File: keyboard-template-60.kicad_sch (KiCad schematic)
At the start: 168 parts, among them J1 USB_C_Receptacle_USB2.0, J2 Conn_01x04_MountingPin, SW1 SW_Reset, U1 ATmega32U4-M, U2 SRV05-4, Y1 16MHz

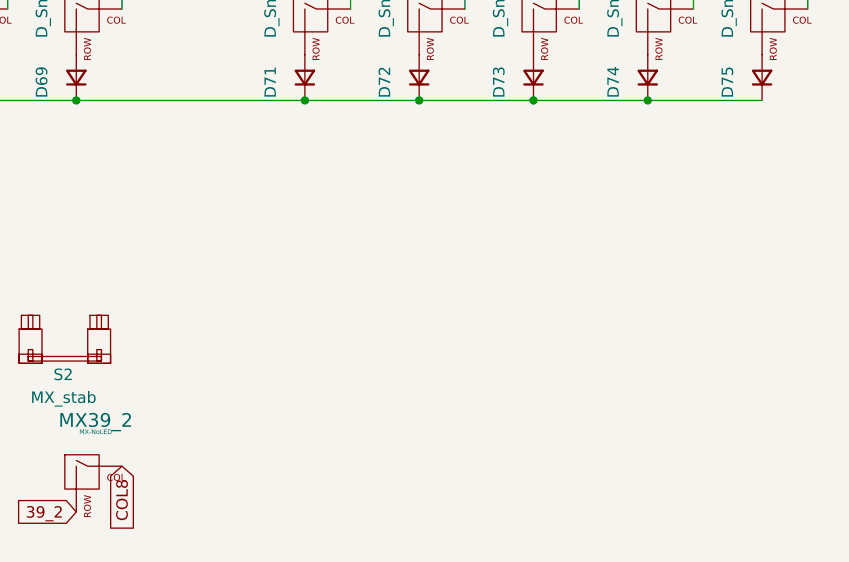
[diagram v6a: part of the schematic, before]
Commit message: Add mounting holes and re-export productions files
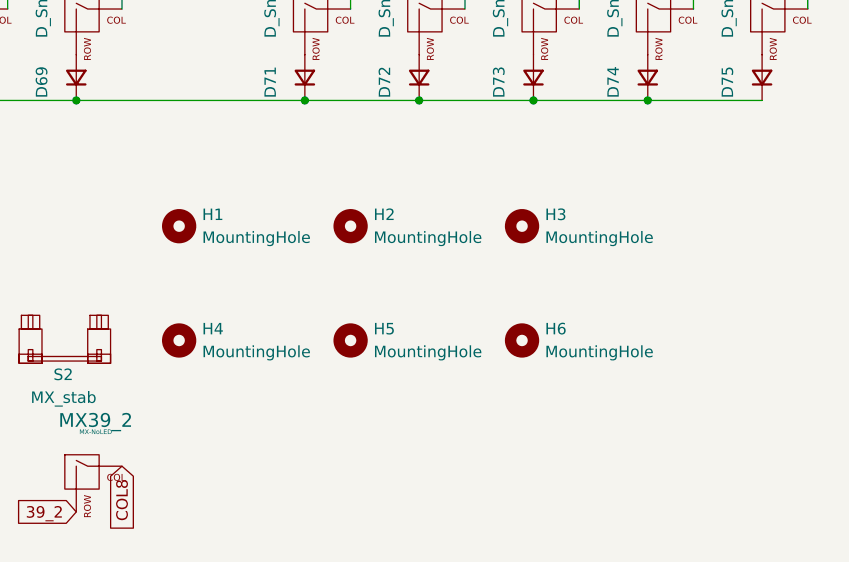
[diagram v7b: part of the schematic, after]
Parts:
- added H1, H2, H3, H4, H5, H6: MountingHole, MountingHole:MountingHole_2.2mm_M2_Pad_TopOnly, symbol Mechanical:MountingHole
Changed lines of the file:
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@@
     (pin "2")
+  )
+  (symbol (lib_id "Mechanical:MountingHole") (at 203.2 241.3 0) (unit 1)
+    (in_bom yes) (on_board yes) (fields_autoplaced)
+    (property "Reference" "H6" (id 0) (at 205.74 240.0299 0)
+      (effects (font (size 1.27 1.27)) (justify left))
+    )
+    (property "Value" "MountingHole" (id 1) (at 205.74 242.5699 0)
+      (effects (font (size 1.27 1.27)) (justify left))
+    )
+    (property "Footprint" "MountingHole:MountingHole_2.2mm_M2_Pad_TopOnly" (id 2) (at 203.2 241.3 0)
+      (effects (font (size 1.27 1.27)) hide)
+    )
+    (property "Datasheet" "~" (id 3) (at 203.2 241.3 0)
+      (effects (font (size 1.27 1.27)) hide)
+    )
   )
   (symbol (lib_id "MX_Alps_Hybrid:MX-NoLED") (at 53.34 129.54 0) (unit 1)
@@
     (pin "1")
     (pin "2")
+  )
+  (symbol (lib_id "Mechanical:MountingHole") (at 165.1 241.3 0) (unit 1)
+    (in_bom yes) (on_board yes) (fields_autoplaced)
+    (property "Reference" "H4" (id 0) (at 167.64 240.0299 0)
+      (effects (font (size 1.27 1.27)) (justify left))
+    )
+    (property "Value" "MountingHole" (id 1) (at 167.64 242.5699 0)
+      (effects (font (size 1.27 1.27)) (justify left))
+    )
+    (property "Footprint" "MountingHole:MountingHole_2.2mm_M2_Pad_TopOnly" (id 2) (at 165.1 241.3 0)
+      (effects (font (size 1.27 1.27)) hide)
+    )
+    (property "Datasheet" "~" (id 3) (at 165.1 241.3 0)
+      (effects (font (size 1.27 1.27)) hide)
+    )
   )
   (symbol (lib_id "Device:D_Small") (at 52.07 59.69 90) (unit 1)
@@
     (pin "1")
     (pin "2")
+  )
+  (symbol (lib_id "Mechanical:MountingHole") (at 184.15 241.3 0) (unit 1)
+    (in_bom yes) (on_board yes) (fields_autoplaced)
+    (property "Reference" "H5" (id 0) (at 186.69 240.0299 0)
+      (effects (font (size 1.27 1.27)) (justify left))
+    )
+    (property "Value" "MountingHole" (id 1) (at 186.69 242.5699 0)
+      (effects (font (size 1.27 1.27)) (justify left))
+    )
+    (property "Footprint" "MountingHole:MountingHole_2.2mm_M2_Pad_TopOnly" (id 2) (at 184.15 241.3 0)
+      (effects (font (size 1.27 1.27)) hide)
+    )
+    (property "Datasheet" "~" (id 3) (at 184.15 241.3 0)
+      (effects (font (size 1.27 1.27)) hide)
+    )
   )
   (symbol (lib_id "Device:C_Small") (at 368.3 165.1 0) (unit 1)
@@
     (pin "2")
   )
+  (symbol (lib_id "Mechanical:MountingHole") (at 203.2 228.6 0) (unit 1)
+    (in_bom yes) (on_board yes) (fields_autoplaced)
+    (property "Reference" "H3" (id 0) (at 205.74 227.3299 0)
+      (effects (font (size 1.27 1.27)) (justify left))
+    )
+    (property "Value" "MountingHole" (id 1) (at 205.74 229.8699 0)
+      (effects (font (size 1.27 1.27)) (justify left))
+    )
+    (property "Footprint" "MountingHole:MountingHole_2.2mm_M2_Pad_TopOnly" (id 2) (at 203.2 228.6 0)
+      (effects (font (size 1.27 1.27)) hide)
+    )
+    (property "Datasheet" "~" (id 3) (at 203.2 228.6 0)
+      (effects (font (size 1.27 1.27)) hide)
+    )
+  )
   (symbol (lib_id "MX_Alps_Hybrid:MX-NoLED") (at 78.74 167.64 0) (unit 1)
     (in_bom yes) (on_board yes) (fields_autoplaced)
@@
     (pin "2")
   )
+  (symbol (lib_id "Mechanical:MountingHole") (at 184.15 228.6 0) (unit 1)
+    (in_bom yes) (on_board yes) (fields_autoplaced)
+    (property "Reference" "H2" (id 0) (at 186.69 227.3299 0)
+      (effects (font (size 1.27 1.27)) (justify left))
+    )
+    (property "Value" "MountingHole" (id 1) (at 186.69 229.8699 0)
+      (effects (font (size 1.27 1.27)) (justify left))
+    )
+    (property "Footprint" "MountingHole:MountingHole_2.2mm_M2_Pad_TopOnly" (id 2) (at 184.15 228.6 0)
+      (effects (font (size 1.27 1.27)) hide)
+    )
+    (property "Datasheet" "~" (id 3) (at 184.15 228.6 0)
+      (effects (font (size 1.27 1.27)) hide)
+    )
+  )
   (symbol (lib_id "MX_Alps_Hybrid:MX-NoLED") (at 129.54 129.54 0) (unit 1)
     (in_bom yes) (on_board yes) (fields_autoplaced)
@@
     (pin "1")
     (pin "2")
+  )
+  (symbol (lib_id "Mechanical:MountingHole") (at 165.1 228.6 0) (unit 1)
+    (in_bom yes) (on_board yes) (fields_autoplaced)
+    (property "Reference" "H1" (id 0) (at 167.64 227.3299 0)
+      (effects (font (size 1.27 1.27)) (justify left))
+    )
+    (property "Value" "MountingHole" (id 1) (at 167.64 229.8699 0)
+      (effects (font (size 1.27 1.27)) (justify left))
+    )
+    (property "Footprint" "MountingHole:MountingHole_2.2mm_M2_Pad_TopOnly" (id 2) (at 165.1 228.6 0)
+      (effects (font (size 1.27 1.27)) hide)
+    )
+    (property "Datasheet" "~" (id 3) (at 165.1 228.6 0)
+      (effects (font (size 1.27 1.27)) hide)
+    )
   )
   (symbol (lib_id "Device:R_Small") (at 381 96.52 90) (unit 1)
@@
       (reference "F1") (unit 1) (value "500mA") (footprint "Fuse:Fuse_1206_3216Metric_Pad1.42x1.75mm_HandSolder")
     )
+    (path "/bcbf2415-a109-4d9c-9e0e-e4b0a2c96713"
+      (reference "H1") (unit 1) (value "MountingHole") (footprint "MountingHole:MountingHole_2.2mm_M2_Pad_TopOnly")
+    )
+    (path "/bba612f2-e838-4991-a0be-649ede51422b"
+      (reference "H2") (unit 1) (value "MountingHole") (footprint "MountingHole:MountingHole_2.2mm_M2_Pad_TopOnly")
+    )
+    (path "/b8b63b67-2a0b-44ac-8bc9-f3859386a147"
+      (reference "H3") (unit 1) (value "MountingHole") (footprint "MountingHole:MountingHole_2.2mm_M2_Pad_TopOnly")
+    )
+    (path "/7eb15e8d-fc12-4b0f-9888-917883d3d39c"
+      (reference "H4") (unit 1) (value "MountingHole") (footprint "MountingHole:MountingHole_2.2mm_M2_Pad_TopOnly")
+    )
+    (path "/892f491a-69c7-4353-b1be-c9694c84502c"
+      (reference "H5") (unit 1) (value "MountingHole") (footprint "MountingHole:MountingHole_2.2mm_M2_Pad_TopOnly")
+    )
+    (path "/7a8541c6-4355-465d-b3ff-c2af755bd664"
+      (reference "H6") (unit 1) (value "MountingHole") (footprint "MountingHole:MountingHole_2.2mm_M2_Pad_TopOnly")
+    )
     (path "/39fd6eec-df64-4ec7-90d9-dff965db8c15"

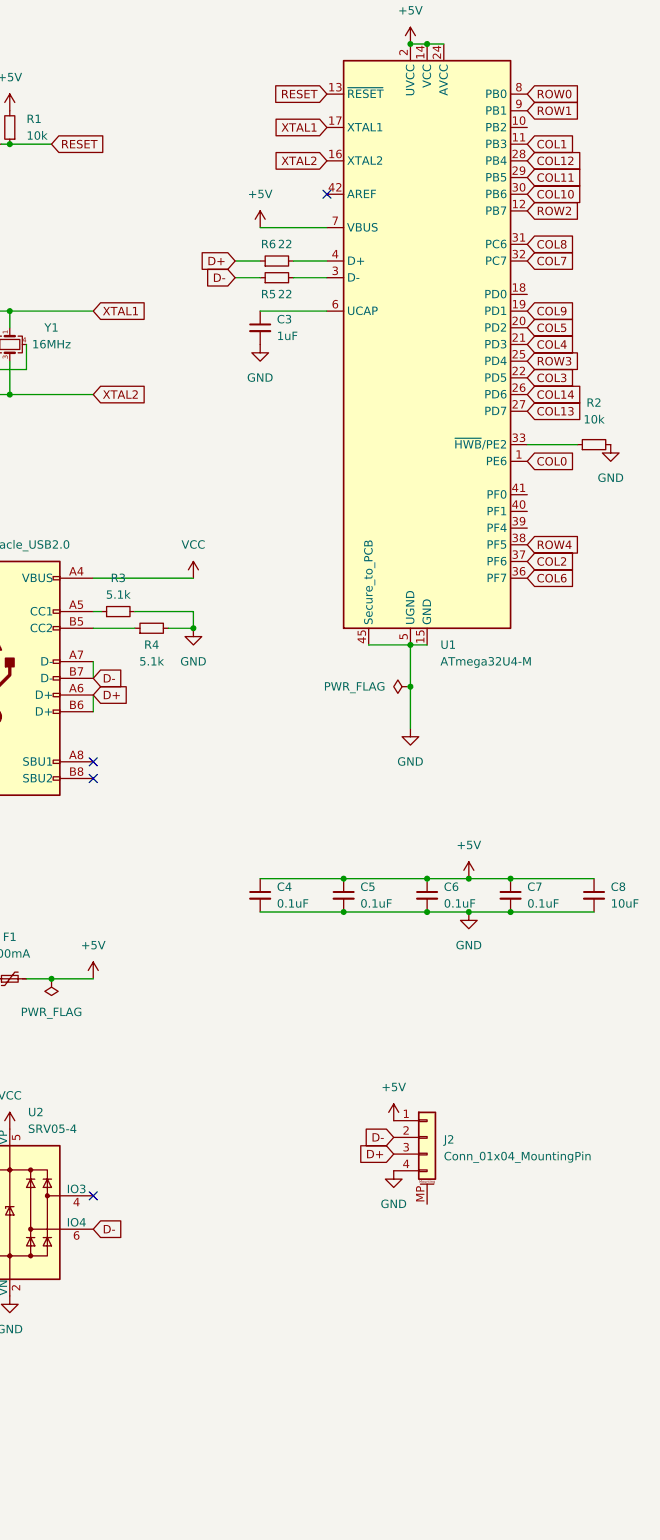
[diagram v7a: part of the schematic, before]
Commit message: SIP socket placement
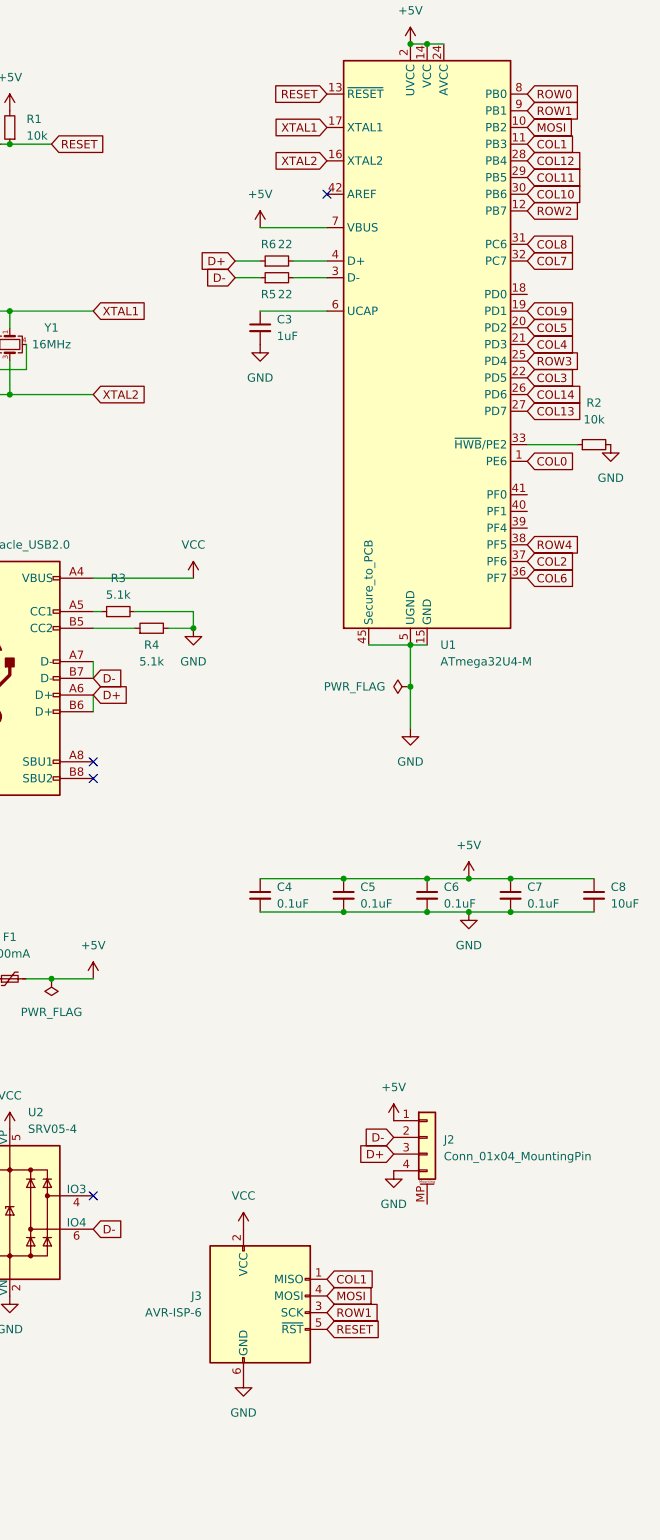
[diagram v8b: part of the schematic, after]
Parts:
- added J3: AVR-ISP-6, Connector_PinHeader_2.54mm:PinHeader_2x03_P2.54mm_Horizontal, symbol Connector:AVR-ISP-6
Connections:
- net COL1: now also J3.1 (MISO)
- net GND: now also J3.6 (GND)
- net RESET: now also J3.5 (~{RST})
- net ROW1: now also J3.3 (SCK)
- net VCC: now also J3.2 (VCC)
- net MOSI: now reaches U1.10 (PB2)
- net MOSI: now also J3.4 (MOSI)
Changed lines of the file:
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@@
     )
   )
+  (global_label "ROW1" (shape input) (at 340.36 228.6 0) (fields_autoplaced)
+    (effects (font (size 1.27 1.27)) (justify left))
+    (property "Intersheet References" "${INTERSHEET_REFS}" (id 0) (at 348.0345 228.6794 0)
+      (effects (font (size 1.27 1.27)) (justify left) hide)
+    )
+  )
   (global_label "ROW3" (shape input) (at 38.1 176.53 180) (fields_autoplaced)
     (effects (font (size 1.27 1.27)) (justify right))
@@
     )
   )
+  (global_label "COL1" (shape input) (at 340.36 223.52 0) (fields_autoplaced)
+    (effects (font (size 1.27 1.27)) (justify left))
+    (property "Intersheet References" "${INTERSHEET_REFS}" (id 0) (at 347.6112 223.5994 0)
+      (effects (font (size 1.27 1.27)) (justify left) hide)
+    )
+  )
   (global_label "COL5" (shape input) (at 120.65 38.1 180) (fields_autoplaced)
     (effects (font (size 1.27 1.27)) (justify right))
@@
     )
   )
+  (global_label "RESET" (shape input) (at 340.36 231.14 0) (fields_autoplaced)
+    (effects (font (size 1.27 1.27)) (justify left))
+    (property "Intersheet References" "${INTERSHEET_REFS}" (id 0) (at 348.5183 231.2194 0)
+      (effects (font (size 1.27 1.27)) (justify left) hide)
+    )
+  )
   (global_label "COL11" (shape input) (at 370.84 55.88 0) (fields_autoplaced)
     (effects (font (size 1.27 1.27)) (justify left))
@@
     )
   )
+  (global_label "MOSI" (shape input) (at 340.36 226.06 0) (fields_autoplaced)
+    (effects (font (size 1.27 1.27)) (justify left))
+    (property "Intersheet References" "${INTERSHEET_REFS}" (id 0) (at 347.3693 225.9806 0)
+      (effects (font (size 1.27 1.27)) (justify left) hide)
+    )
+  )
   (global_label "COL12" (shape input) (at 209.55 38.1 180) (fields_autoplaced)
     (effects (font (size 1.27 1.27)) (justify right))
@@
     )
   )
+  (global_label "MOSI" (shape input) (at 370.84 48.26 0) (fields_autoplaced)
+    (effects (font (size 1.27 1.27)) (justify left))
+    (property "Intersheet References" "${INTERSHEET_REFS}" (id 0) (at 377.8493 48.1806 0)
+      (effects (font (size 1.27 1.27)) (justify left) hide)
+    )
+  )
   (global_label "ROW2" (shape input) (at 370.84 60.96 0) (fields_autoplaced)
     (effects (font (size 1.27 1.27)) (justify left))
@@
     (pin "2")
   )
+  (symbol (lib_id "power:VCC") (at 327.66 215.9 0) (unit 1)
+    (in_bom yes) (on_board yes) (fields_autoplaced)
+    (property "Reference" "#PWR0101" (id 0) (at 327.66 219.71 0)
+      (effects (font (size 1.27 1.27)) hide)
+    )
+    (property "Value" "VCC" (id 1) (at 327.66 210.82 0))
+    (property "Footprint" "" (id 2) (at 327.66 215.9 0)
+      (effects (font (size 1.27 1.27)) hide)
+    )
+    (property "Datasheet" "" (id 3) (at 327.66 215.9 0)
+      (effects (font (size 1.27 1.27)) hide)
+    )
+    (pin "1")
+  )
   (symbol (lib_id "MX_Alps_Hybrid:MX-NoLED") (at 218.44 205.74 0) (unit 1)
     (in_bom yes) (on_board yes) (fields_autoplaced)
@@
     (pin "2")
   )
+  (symbol (lib_id "Connector:AVR-ISP-6") (at 330.2 228.6 0) (unit 1)
+    (in_bom yes) (on_board yes) (fields_autoplaced)
+    (property "Reference" "J3" (id 0) (at 321.31 226.0599 0)
+      (effects (font (size 1.27 1.27)) (justify right))
+    )
+    (property "Value" "AVR-ISP-6" (id 1) (at 321.31 228.5999 0)
+      (effects (font (size 1.27 1.27)) (justify right))
+    )
+    (property "Footprint" "Connector_PinHeader_2.54mm:PinHeader_2x03_P2.54mm_Horizontal" (id 2) (at 323.85 227.33 90)
+      (effects (font (size 1.27 1.27)) hide)
+    )
+    (property "Datasheet" " ~" (id 3) (at 297.815 242.57 0)
+      (effects (font (size 1.27 1.27)) hide)
+    )
+    (pin "1")
+    (pin "2")
+    (pin "3")
+    (pin "4")
+    (pin "5")
+    (pin "6")
+  )
   (symbol (lib_id "MX_Alps_Hybrid:MX-NoLED") (at 116.84 129.54 0) (unit 1)
     (in_bom yes) (on_board yes) (fields_autoplaced)
@@
     (pin "2")
   )
+  (symbol (lib_id "power:GND") (at 327.66 238.76 0) (unit 1)
+    (in_bom yes) (on_board yes)
+    (property "Reference" "#PWR0102" (id 0) (at 327.66 245.11 0)
+      (effects (font (size 1.27 1.27)) hide)
+    )
+    (property "Value" "GND" (id 1) (at 327.66 243.84 0))
+    (property "Footprint" "" (id 2) (at 327.66 238.76 0)
+      (effects (font (size 1.27 1.27)) hide)
+    )
+    (property "Datasheet" "" (id 3) (at 327.66 238.76 0)
+      (effects (font (size 1.27 1.27)) hide)
+    )
+    (pin "1")
+  )
   (symbol (lib_id "MX_Alps_Hybrid:MX-NoLED") (at 78.74 205.74 0) (unit 1)
     (in_bom yes) (on_board yes) (fields_autoplaced)
@@
       (reference "#PWR019") (unit 1) (value "GND") (footprint "")
     )
+    (path "/4f697800-378f-46d2-9e80-4b01ffa24474"
+      (reference "#PWR0101") (unit 1) (value "VCC") (footprint "")
+    )
+    (path "/f962a143-99d3-4467-a1c1-6618d8ad349c"
+      (reference "#PWR0102") (unit 1) (value "GND") (footprint "")
+    )
     (path "/0d4e228a-908e-4dad-a056-e4214b8aa2b1"
       (reference "C1") (unit 1) (value "22pF") (footprint "Capacitor_SMD:C_0603_1608Metric_Pad1.08x0.95mm_HandSolder")
@@
       (reference "J2") (unit 1) (value "Conn_01x04_MountingPin") (footprint "Connector_JST:JST_ACH_BM04B-ACHSS-A-GAN-ETF_1x04-1MP_P1.20mm_Vertical")
     )
+    (path "/777de625-89f8-4e2e-9121-2fba386d4e70"
+      (reference "J3") (unit 1) (value "AVR-ISP-6") (footprint "Connector_PinHeader_2.54mm:PinHeader_2x03_P2.54mm_Horizontal")
+    )
     (path "/bb3a180f-cdbc-49d0-97a9-6846eb214c84"
